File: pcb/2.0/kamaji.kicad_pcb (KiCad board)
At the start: 2 copper layers, 100 x 100 mm, 64 parts, among them J1 RJ10, J2 RJ10, J3 RJ10, J4 RJ10, J5 RJ10, J6 RJ10, J7 USB_B, J8 USB_A, Q1 2N3904, Q2 IRL540N, Q3 IRL540N, SW1 SW_Push, SW2 SW_Push, SW3 SW_Push, U1 ATMEGA32U4-AU, Y1 16MHz

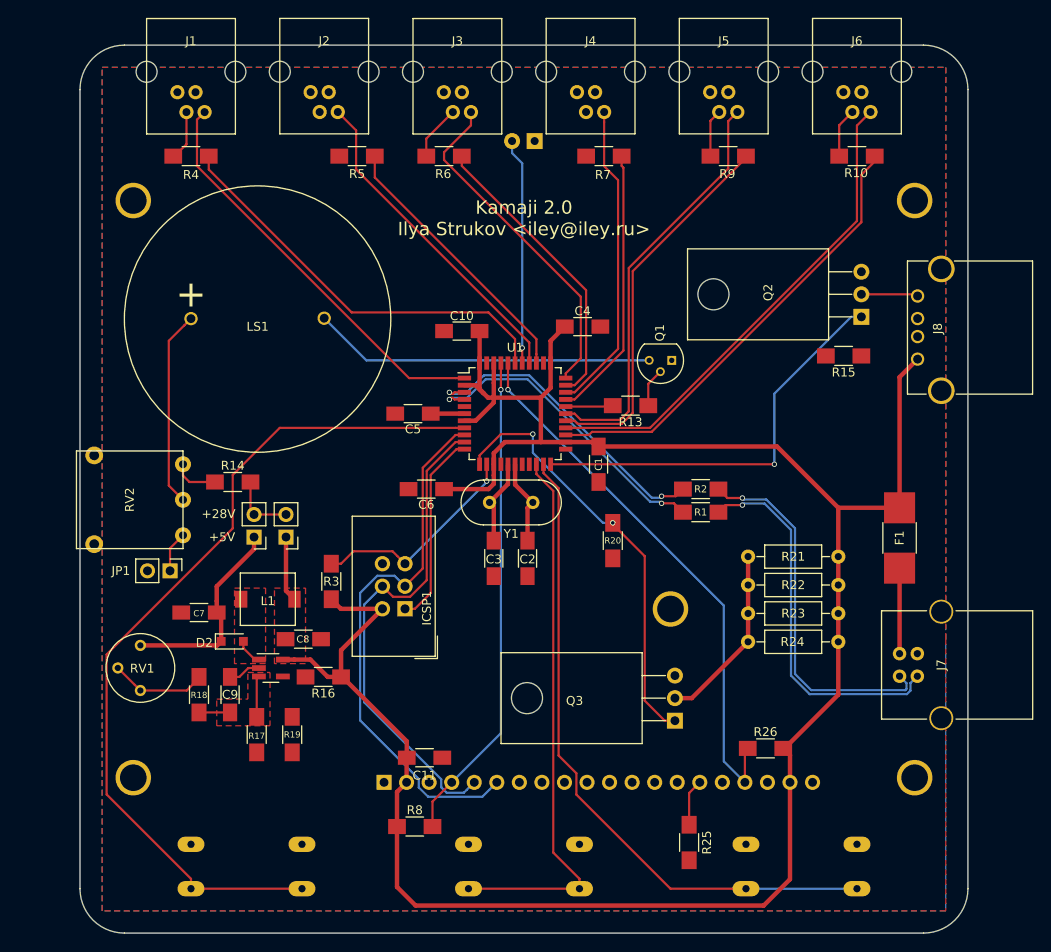
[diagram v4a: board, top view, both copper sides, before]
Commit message: change socket and potentiometer footprints
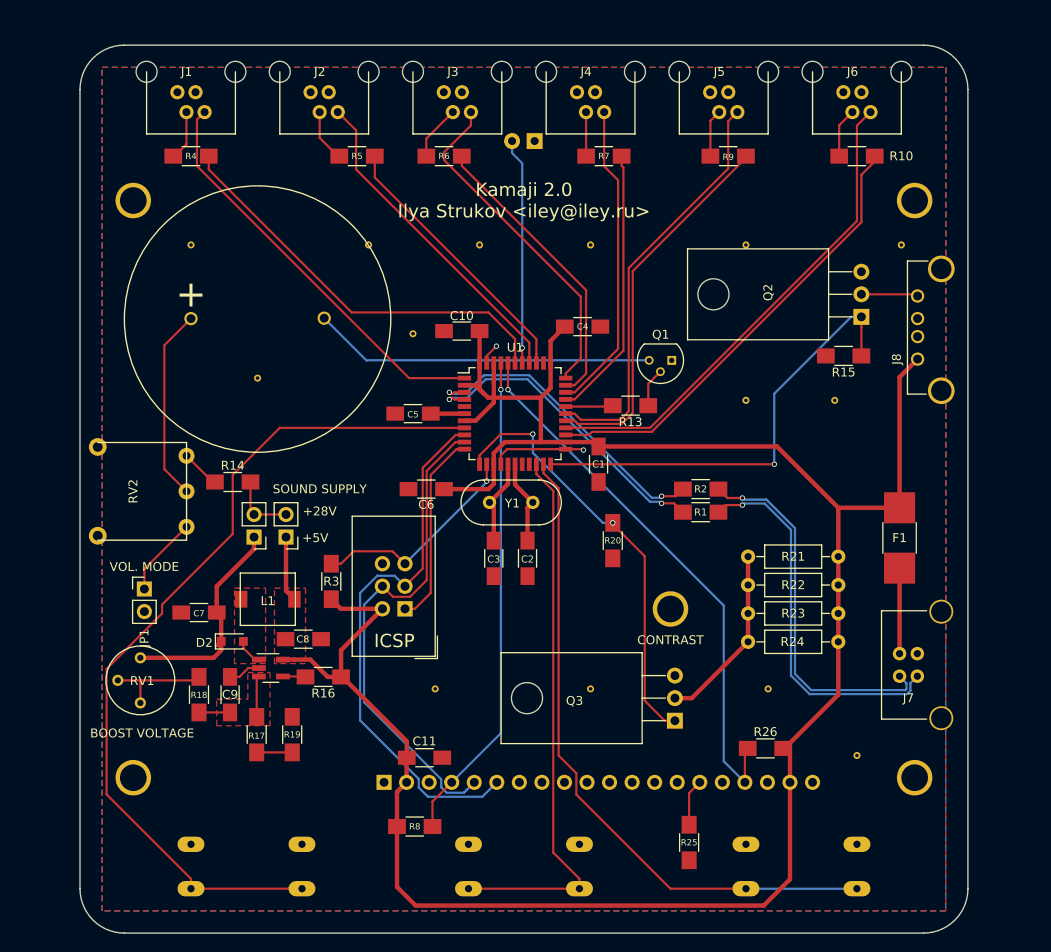
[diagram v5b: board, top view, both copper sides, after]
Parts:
- added VIA**: Via_0.8mm, kamaji:Via_0.8mm, F.Cu at (90.0, 122.5)
- added VIA**: Via_0.8mm, kamaji:Via_0.8mm, F.Cu at (62.5, 72.5)
- added VIA**: Via_0.8mm, kamaji:Via_0.8mm, F.Cu at (125.0, 72.5)
- added VIA**: Via_0.8mm, kamaji:Via_0.8mm, F.Cu at (107.5, 72.5)
- added VIA**: Via_0.8mm, kamaji:Via_0.8mm, F.Cu at (95.0, 72.5)
- added VIA**: Via_0.8mm, kamaji:Via_0.8mm, F.Cu at (82.5, 72.5)
- added VIA**: Via_0.8mm, kamaji:Via_0.8mm, F.Cu at (107.5, 122.5)
- added VIA**: Via_0.8mm, kamaji:Via_0.8mm, F.Cu at (127.5, 122.5)
- added VIA**: Via_0.8mm, kamaji:Via_0.8mm, F.Cu at (137.5, 130.0)
- added VIA**: Via_0.8mm, kamaji:Via_0.8mm, F.Cu at (142.5, 72.5)
- added VIA**: Via_0.8mm, kamaji:Via_0.8mm, F.Cu at (135.0, 90.0)
- added VIA**: Via_0.8mm, kamaji:Via_0.8mm, F.Cu at (125.0, 90.0)
- added VIA**: Via_0.8mm, kamaji:Via_0.8mm, F.Cu at (87.5, 82.5)
- added VIA**: Via_0.8mm, kamaji:Via_0.8mm, F.Cu at (70.0, 87.5)
- J7: footprint Connectors:USB_B -> kamaji:USB_B
- J8: footprint Connectors:USB_A -> kamaji:USB_A
- moved JP1 3.54 mm to (57.2, 111.2), turned to 0 degrees
- moved RV1 1.40 mm to (56.8, 124.1)
- moved RV2 1.03 mm to (56.0, 100.2)
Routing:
- net GND: track 3.66 -> 16.7 mm, vias 0 -> 2
- net Net-(J2-Pad2): track 0.00 -> 5.97 mm
- net Net-(J4-Pad2): track 0.00 -> 4.97 mm
- net /LAMP: track 46.5 -> 50.9 mm
- net Net-(JP1-Pad1): track 4.60 -> 8.97 mm
- net Net-(R17-Pad1): track 0.00 -> 4.00 mm
- net Net-(BC1-Pad4): track 0.00 -> 2.57 mm
- net /Boost Converter/BOOST_VOUT: track 23.0 -> 24.8 mm
- net Net-(R18-Pad2): track 10.9 -> 12.0 mm
- net Net-(R14-Pad1): track 5.17 -> 4.42 mm
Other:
- board text added: "BOOST VOLTAGE"
- board text added: "CONTRAST"
- board text added: "ICSP"
- board text added: "SOUND SUPPLY"
- board text added: "VOL. MODE"

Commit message: add mounting holes
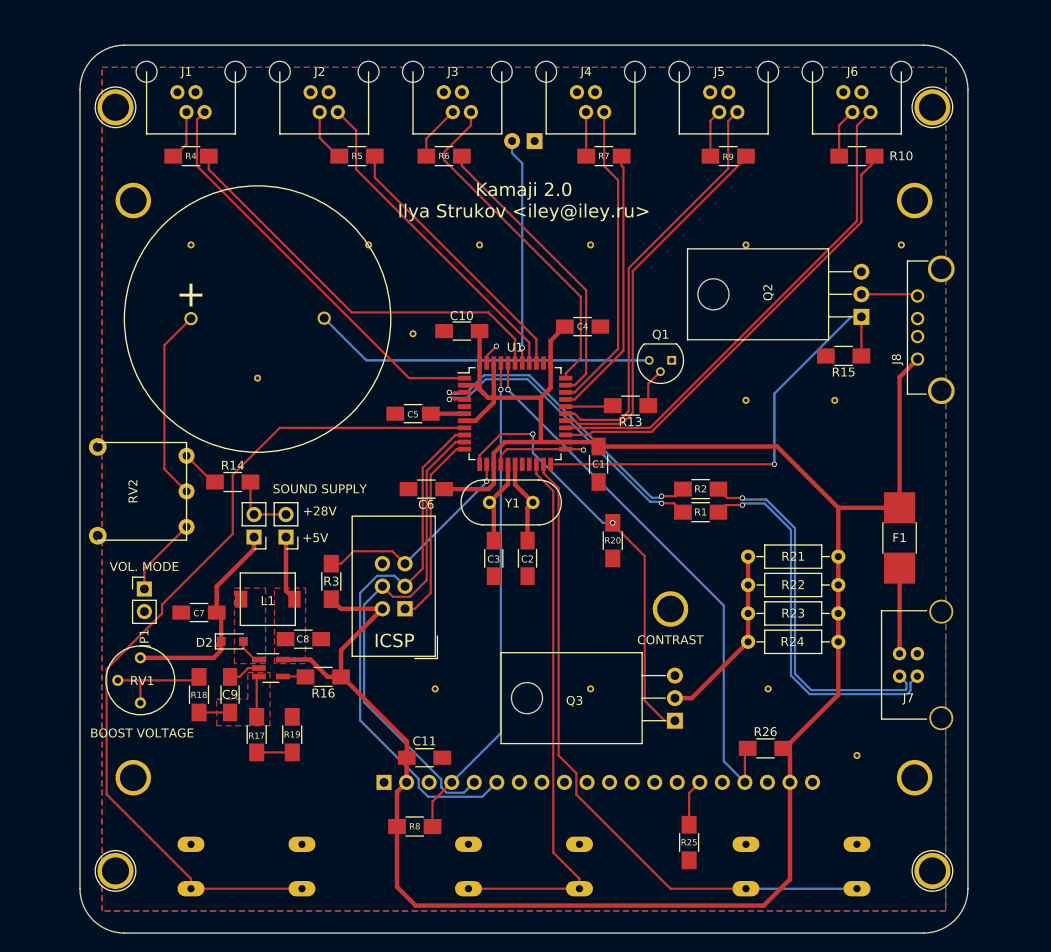
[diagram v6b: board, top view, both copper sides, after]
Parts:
- added REF**: 1pin, Connectors:1pin, F.Cu at (54.0, 57.0)
- added REF**: 1pin, Connectors:1pin, F.Cu at (146.0, 57.0)
- added REF**: 1pin, Connectors:1pin, F.Cu at (54.0, 143.0)
- added REF**: 1pin, Connectors:1pin, F.Cu at (146.0, 143.0)
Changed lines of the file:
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@@
 (kicad_pcb (version 4) (host pcbnew 4.0.7)
   (general
-    (links 177)
+    (links 0)
     (no_connects 0)
     (area 49.924999 49.924999 150.075001 150.075001)
@@
     (tracks 380)
     (zones 0)
-    (modules 78)
+    (modules 82)
     (nets 57)
   )
@@
     (mod_text_size 1 1)
     (mod_text_width 0.15)
-    (pad_size 0.8 0.8)
-    (pad_drill 0.4)
+    (pad_size 4.064 4.064)
+    (pad_drill 3.048)
     (pad_to_mask_clearance 0.2)
     (aux_axis_origin 0 0)
@@
     (add_net VCC)
   )
+  (module Connectors:1pin (layer F.Cu)
+    (at 54 57)
+    (descr "module 1 pin (ou trou mecanique de percage)")
+    (tags DEV)
+    (fp_text reference REF** (at 0 -3.048) (layer F.SilkS) hide
+      (effects (font (size 1 1) (thickness 0.15)))
+    )
+    (fp_text value 1pin (at 0 3) (layer F.Fab)
+      (effects (font (size 1 1) (thickness 0.15)))
+    )
+    (fp_circle (center 0 0) (end 2 0.8) (layer F.Fab) (width 0.1))
+    (fp_circle (center 0 0) (end 2.6 0) (layer F.CrtYd) (width 0.05))
+    (fp_circle (center 0 0) (end 0 -2.286) (layer F.SilkS) (width 0.12))
+    (pad "" np_thru_hole circle (at 0 0) (size 4.064 4.064) (drill 3.048) (layers *.Cu *.Mask))
+  )
+  (module Connectors:1pin (layer F.Cu)
+    (at 146 57)
+    (descr "module 1 pin (ou trou mecanique de percage)")
+    (tags DEV)
+    (fp_text reference REF** (at 0 -3.048) (layer F.SilkS) hide
+      (effects (font (size 1 1) (thickness 0.15)))
+    )
+    (fp_text value 1pin (at 0 3) (layer F.Fab)
+      (effects (font (size 1 1) (thickness 0.15)))
+    )
+    (fp_circle (center 0 0) (end 2 0.8) (layer F.Fab) (width 0.1))
+    (fp_circle (center 0 0) (end 2.6 0) (layer F.CrtYd) (width 0.05))
+    (fp_circle (center 0 0) (end 0 -2.286) (layer F.SilkS) (width 0.12))
+    (pad "" np_thru_hole circle (at 0 0) (size 4.064 4.064) (drill 3.048) (layers *.Cu *.Mask))
+  )
+  (module Connectors:1pin (layer F.Cu)
+    (at 54 143)
+    (descr "module 1 pin (ou trou mecanique de percage)")
+    (tags DEV)
+    (fp_text reference REF** (at 0 -3.048) (layer F.SilkS) hide
+      (effects (font (size 1 1) (thickness 0.15)))
+    )
+    (fp_text value 1pin (at 0 3) (layer F.Fab)
+      (effects (font (size 1 1) (thickness 0.15)))
+    )
+    (fp_circle (center 0 0) (end 2 0.8) (layer F.Fab) (width 0.1))
+    (fp_circle (center 0 0) (end 2.6 0) (layer F.CrtYd) (width 0.05))
+    (fp_circle (center 0 0) (end 0 -2.286) (layer F.SilkS) (width 0.12))
+    (pad "" np_thru_hole circle (at 0 0) (size 4.064 4.064) (drill 3.048) (layers *.Cu *.Mask))
+  )
   (module kamaji:Via_0.8mm (layer F.Cu)
     (at 90 122.5)
@@
     (pad "" np_thru_hole circle (at 5 -4 90) (size 2 2) (drill 1.1) (layers *.Cu *.Mask))
   )
+  (module Connectors:1pin (layer F.Cu)
+    (at 146 143)
+    (descr "module 1 pin (ou trou mecanique de percage)")
+    (tags DEV)
+    (fp_text reference REF** (at 0 -3.048) (layer F.SilkS) hide
+      (effects (font (size 1 1) (thickness 0.15)))
+    )
+    (fp_text value 1pin (at 0 3) (layer F.Fab)
+      (effects (font (size 1 1) (thickness 0.15)))
+    )
+    (fp_circle (center 0 0) (end 2 0.8) (layer F.Fab) (width 0.1))
+    (fp_circle (center 0 0) (end 2.6 0) (layer F.CrtYd) (width 0.05))
+    (fp_circle (center 0 0) (end 0 -2.286) (layer F.SilkS) (width 0.12))
+    (pad "" np_thru_hole circle (at 0 0) (size 4.064 4.064) (drill 3.048) (layers *.Cu *.Mask))
+  )
   (gr_text CONTRAST (at 116.5 117) (layer F.SilkS)
